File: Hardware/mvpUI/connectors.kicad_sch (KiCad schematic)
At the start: 16 parts, among them J2 54-00305, J3 MEM2061-01-188-00-A_REVA, J4 503566-2102, U4 74LVC1GU04DRL

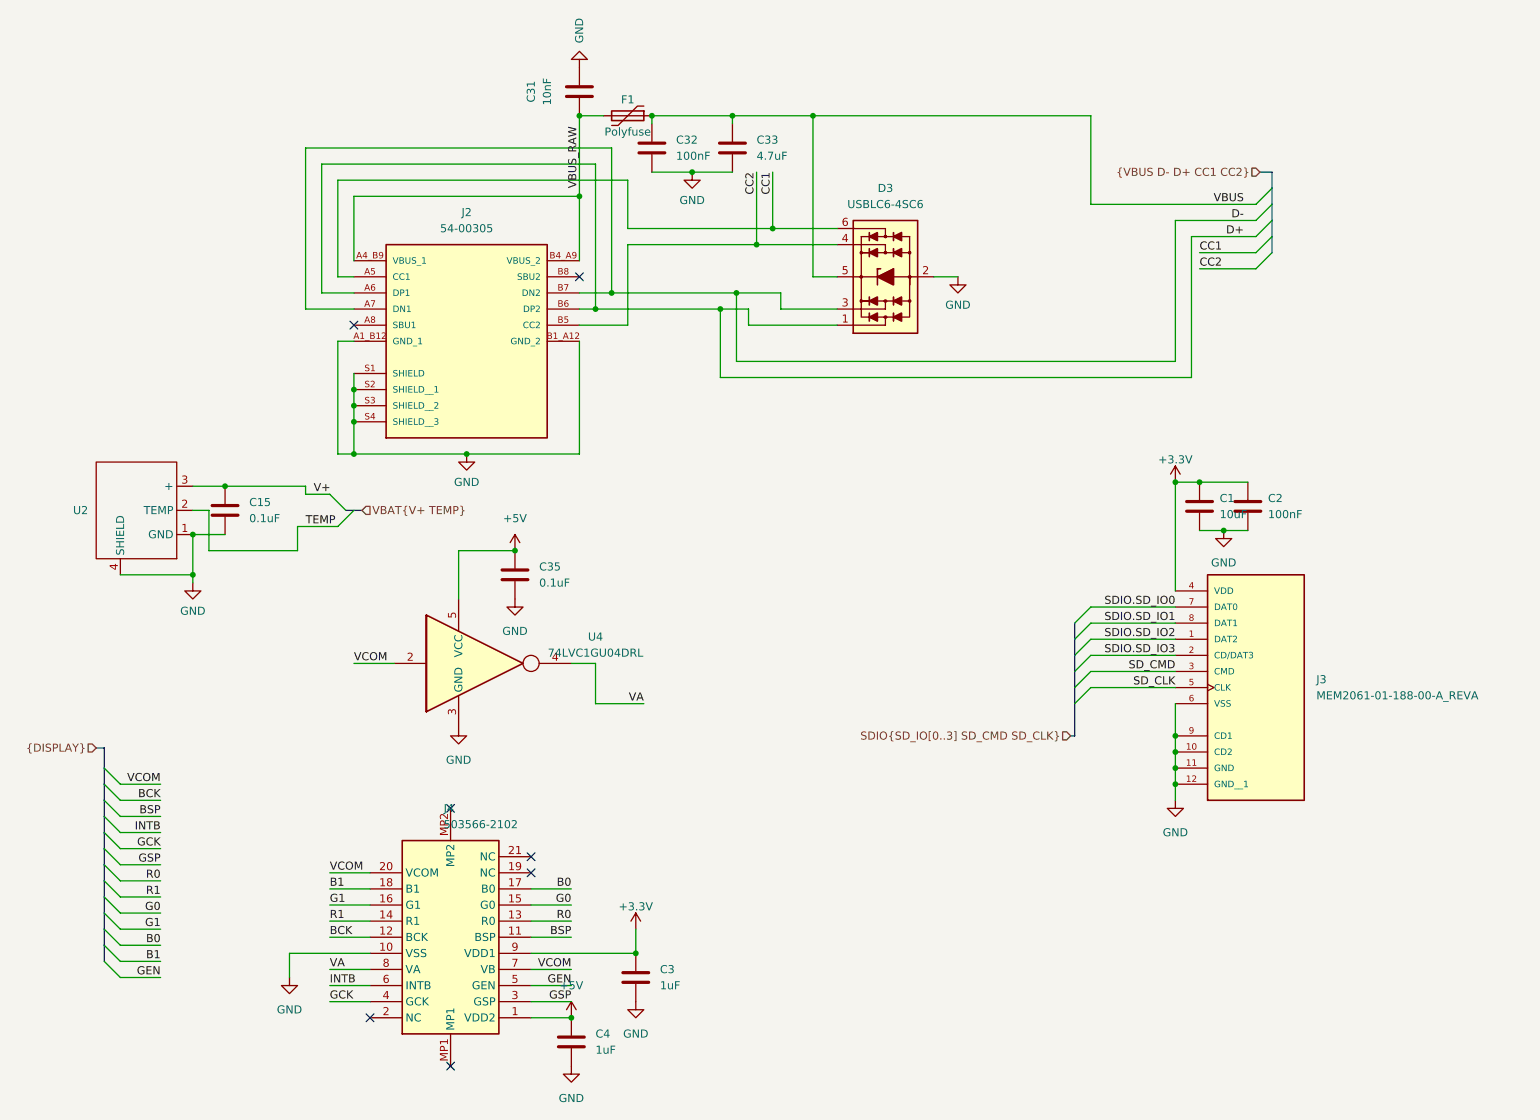
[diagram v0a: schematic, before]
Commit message: Getting there...
Just need logic and power planes for the most part (and verify everything once more)
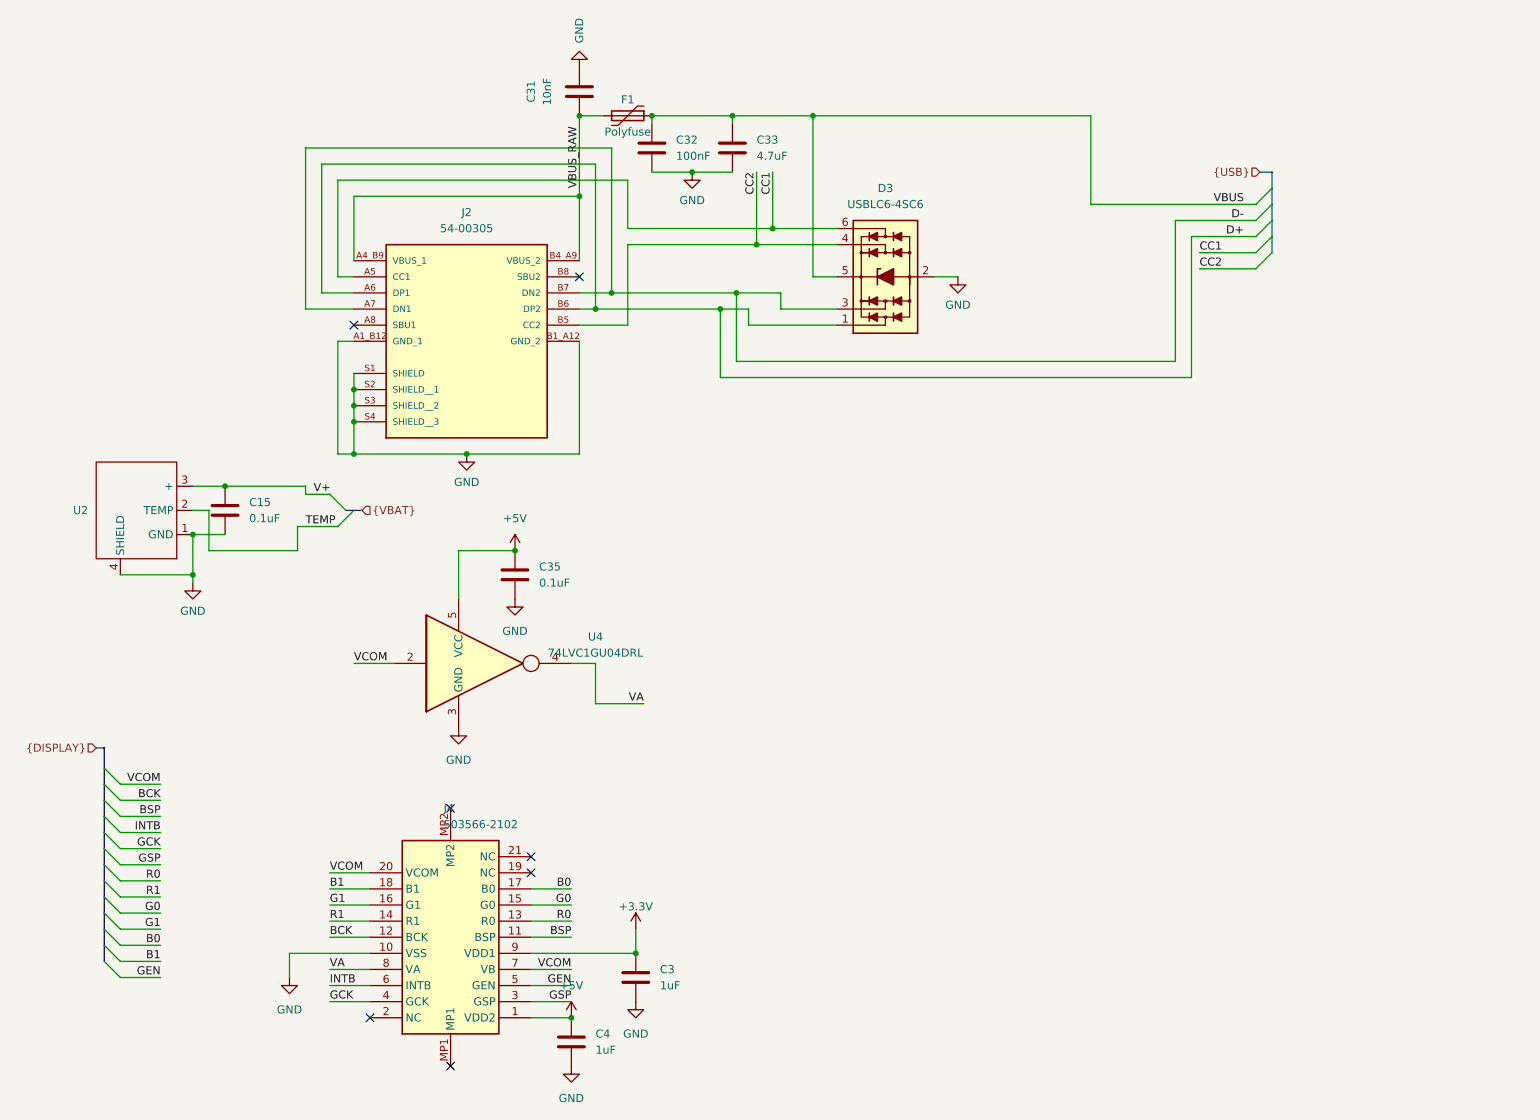
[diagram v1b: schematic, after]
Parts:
- removed C1: 10uF, Capacitor_SMD_US_Handsoldering_AKL:C_0603_1608Metric, symbol Device:C
- removed C2: 100nF, Capacitor_SMD_US_Handsoldering_AKL:C_0603_1608Metric, symbol Device:C
- removed J3: MEM2061-01-188-00-A_REVA, phone:GCT_MEM2061-01-188-00-A_REVA, symbol MEM2061-01-188-00-A_REVA:MEM2061-01-188-00-A_REVA

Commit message: Fixed Obvious Dumb
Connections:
- net D+: now also D3.3 (L2); no longer D3.1 (L1)
- net D-: now also D3.1 (L1); no longer D3.3 (L2)
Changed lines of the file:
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@@
     (stroke (width 0) (type default))
   )
-  (wire (pts (xy 151.13 54.61) (xy 151.13 57.15))
-    (stroke (width 0) (type default))
-  )
-  (wire (pts (xy 151.13 57.15) (xy 160.02 57.15))
+  (wire (pts (xy 151.13 54.61) (xy 151.13 59.69))
     (stroke (width 0) (type default))
   )
@@
   )
   (wire (pts (xy 58.42 92.71) (xy 63.5 92.71))
-    (stroke (width 0) (type default))
-  )
-  (wire (pts (xy 146.05 59.69) (xy 160.02 59.69))
     (stroke (width 0) (type default))
   )
@@
     (stroke (width 0) (type default))
   )
-  (wire (pts (xy 141.605 57.15) (xy 146.05 57.15))
+  (wire (pts (xy 141.605 57.15) (xy 160.02 57.15))
     (stroke (width 0) (type default))
   )
@@
     (stroke (width 0) (type default))
   )
-  (wire (pts (xy 146.05 57.15) (xy 146.05 59.69))
-    (stroke (width 0) (type default))
-  )
   (bus (pts (xy 44.45 139.7) (xy 44.45 142.24))
     (stroke (width 0) (type default))
@@
     (stroke (width 0) (type default))
   )
+  (wire (pts (xy 151.13 59.69) (xy 160.02 59.69))
+    (stroke (width 0) (type default))
+  )

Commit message: Production!
Forgot to commit the final, lets hope this works. Also start on software using Slint. Prototype in Plasticity on a free trial to test.
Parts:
- C32: value 100nF -> 0.1uF
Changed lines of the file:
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@@
       (effects (font (size 1.27 1.27)) (justify right))
     )
-    (property "Value" "100nF" (at 134.62 33.02 0)
+    (property "Value" "0.1uF" (at 134.62 33.02 0)
       (effects (font (size 1.27 1.27)) (justify right))
     )
